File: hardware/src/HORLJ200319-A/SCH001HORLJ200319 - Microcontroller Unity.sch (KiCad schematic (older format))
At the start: 14 parts, among them U1 ATmega328P-MMH, Y1 32.768kHz

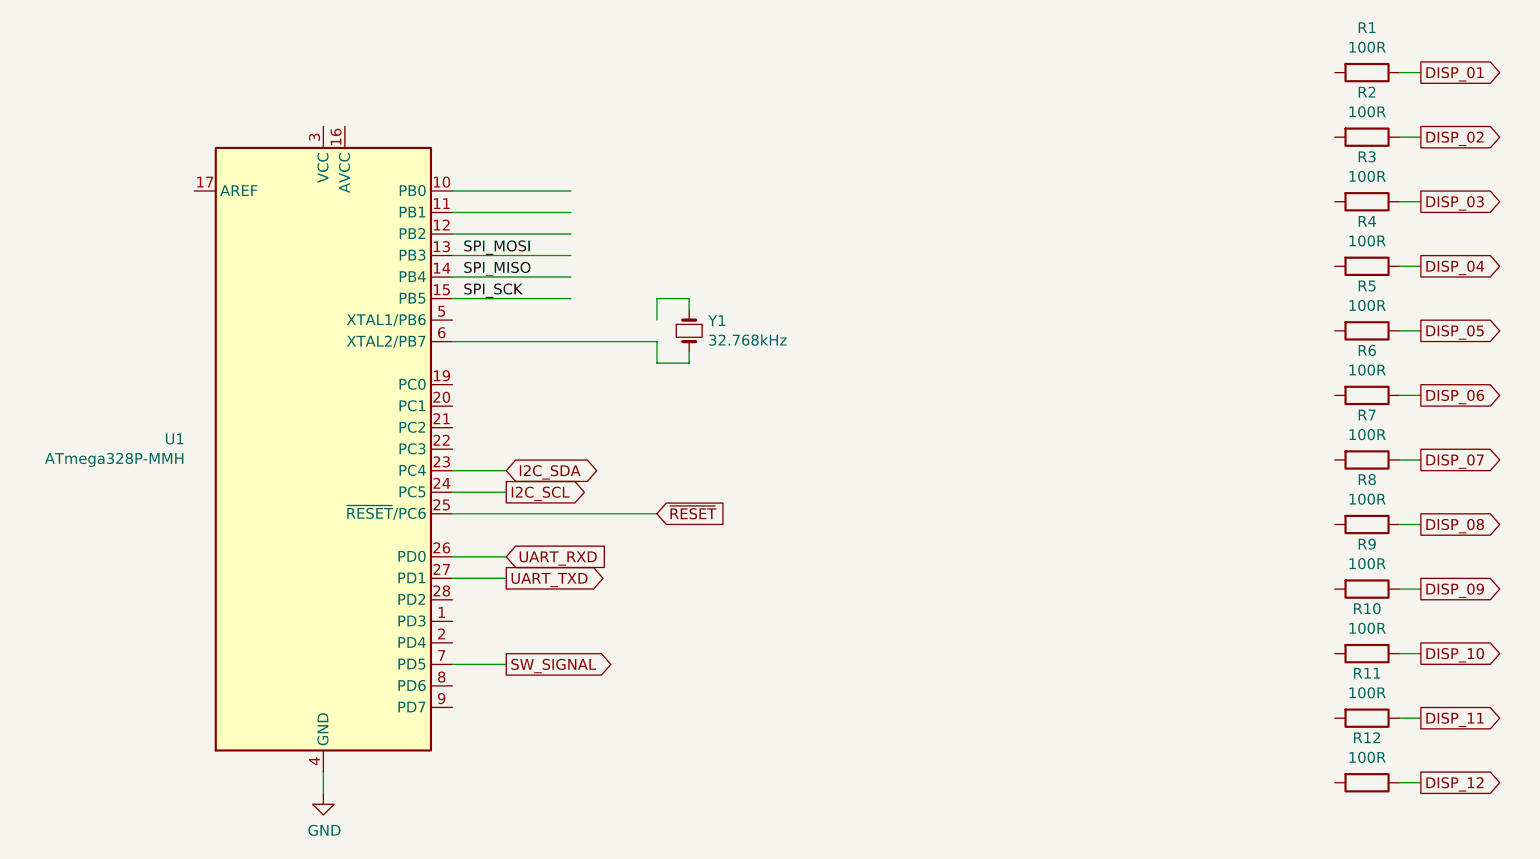
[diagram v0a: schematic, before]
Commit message: Insere MockUps digitais e inicia o projeto da PCB.
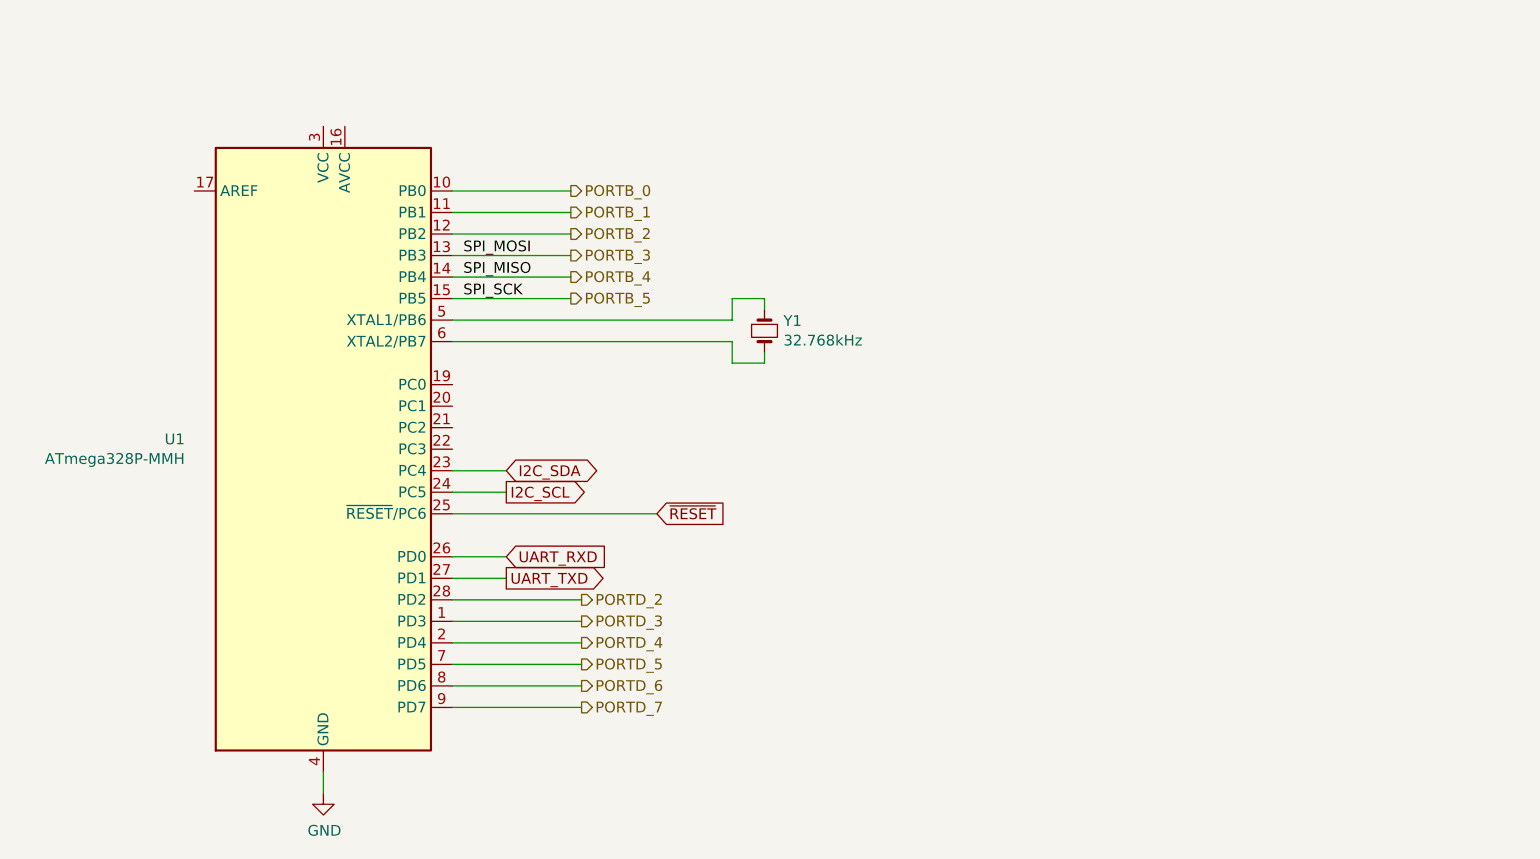
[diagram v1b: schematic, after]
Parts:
- removed R1, R10, R11, R12, R2, R3, R4, R5, R6, R7, R8, R9: 100R, symbol Device:R
- Y1: footprint (none) -> Crystal:Crystal_C26-LF_D2.1mm_L6.5mm_Horizontal
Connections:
- net labels added: PORTB_0, PORTB_1, PORTB_2, PORTB_3, PORTB_4, PORTB_5, PORTD_2, PORTD_3, PORTD_4, PORTD_5, PORTD_6, PORTD_7
- net labels removed: DISP_01, DISP_02, DISP_03, DISP_04, DISP_05, DISP_06, DISP_07, DISP_08, DISP_09, DISP_10, DISP_11, DISP_12, SW_SIGNAL
- wire segments 32 -> 26
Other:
- moved on the sheet: Y1
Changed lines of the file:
@@
 $Descr A4 11693 8268
 encoding utf-8
-Sheet 3 10
+Sheet 2 10
 Title ""
 Date ""
@@
 	1    0    0    -1
 $EndComp
-$Comp
-L Device:Crystal_Small Y1
-U 1 1 5E76C625
-P 5200 3350
-F 0 "Y1" V 5154 3438 50  0000 L CNN
-F 1 "32.768kHz" V 5245 3438 50  0000 L CNN
-F 2 "" H 5200 3350 50  0001 C CNN
-F 3 "~" H 5200 3350 50  0001 C CNN
-	1    5200 3350
-	0    1    1    0
-$EndComp
 Wire Wire Line
-	5050 3300 5050 3200
+	5400 3300 5400 3200
 Wire Wire Line
-	4100 3400 5050 3400
+	4100 3400 5400 3400
 Wire Wire Line
-	5200 3250 5200 3200
+	5550 3200 5400 3200
 Wire Wire Line
-	5200 3200 5050 3200
+	5400 3500 5550 3500
 Wire Wire Line
-	5050 3500 5200 3500
-Wire Wire Line
-	5200 3500 5200 3450
-Wire Wire Line
-	5050 3400 5050 3500
+	5400 3400 5400 3500
 Wire Wire Line
 	4100 4200 5050 4200
@@
 Text GLabel 5050 4200 2    50   Input ~ 0
 ~RESET
-Text GLabel 8600 3050 2    50   Output ~ 0
-DISP_04
-Text GLabel 8600 3350 2    50   Output ~ 0
-DISP_05
-Text GLabel 8600 3650 2    50   Output ~ 0
-DISP_06
 Wire Wire Line
 	4650 3200 4100 3200
@@
 Wire Wire Line
 	4650 3000 4100 3000
-Text GLabel 8600 2150 2    50   Output ~ 0
-DISP_01
 Wire Wire Line
 	4650 2700 4100 2700
-Text GLabel 8600 2450 2    50   Output ~ 0
-DISP_02
 Wire Wire Line
 	4100 2800 4650 2800
-Text GLabel 8600 2750 2    50   Output ~ 0
-DISP_03
 Wire Wire Line
 	4650 2900 4100 2900
@@
 Text Label 4150 3200 0    50   ~ 0
 SPI_SCK
+Text HLabel 4650 2700 2    50   Output ~ 0
+PORTB_0
+Text HLabel 4650 2800 2    50   Output ~ 0
+PORTB_1
+Text HLabel 4650 2900 2    50   Output ~ 0
+PORTB_2
+Text HLabel 4650 3000 2    50   Output ~ 0
+PORTB_3
+Text HLabel 4650 3100 2    50   Output ~ 0
+PORTB_4
+Text HLabel 4650 3200 2    50   Output ~ 0
+PORTB_5
 Wire Wire Line
-	4350 4900 4100 4900
-Text GLabel 4350 4900 2    50   Output ~ 0
-SW_SIGNAL
+	4100 3300 5400 3300
+Wire Wire Line
+	5550 3500 5550 3450
+Wire Wire Line
+	5550 3250 5550 3200
 $Comp
-L Device:R R1
-U 1 1 5E77952B
-P 8350 2150
-F 0 "R1" V 8143 2150 50  0000 C CNN
-F 1 "100R" V 8234 2150 50  0000 C CNN
-F 2 "" V 8280 2150 50  0001 C CNN
-F 3 "~" H 8350 2150 50  0001 C CNN
-	1    8350 2150
+L Device:Crystal_Small Y1
+U 1 1 5E76C625
+P 5550 3350
+F 0 "Y1" V 5504 3438 50  0000 L CNN
+F 1 "32.768kHz" V 5595 3438 50  0000 L CNN
+F 2 "Crystal:Crystal_C26-LF_D2.1mm_L6.5mm_Horizontal" H 5550 3350 50  0001 C CNN
+F 3 "~" H 5550 3350 50  0001 C CNN
+	1    5550 3350
 	0    1    1    0
 $EndComp
+Text HLabel 4700 4600 2    50   Output ~ 0
+PORTD_2
+Text HLabel 4700 4700 2    50   Output ~ 0
+PORTD_3
+Text HLabel 4700 4800 2    50   Output ~ 0
+PORTD_4
+Text HLabel 4700 4900 2    50   Output ~ 0
+PORTD_5
+Text HLabel 4700 5000 2    50   Output ~ 0
+PORTD_6
+Text HLabel 4700 5100 2    50   Output ~ 0
+PORTD_7
 Wire Wire Line
-	8600 2150 8500 2150
-$Comp
-L Device:R R2
-U 1 1 5E779E23
-P 8350 2450
-F 0 "R2" V 8143 2450 50  0000 C CNN
-F 1 "100R" V 8234 2450 50  0000 C CNN
-F 2 "" V 8280 2450 50  0001 C CNN
-F 3 "~" H 8350 2450 50  0001 C CNN
-	1    8350 2450
-	0    1    1    0
-$EndComp
-$Comp
-L Device:R R3
-U 1 1 5E77A0CA
-P 8350 2750
-F 0 "R3" V 8143 2750 50  0000 C CNN
-F 1 "100R" V 8234 2750 50  0000 C CNN
-F 2 "" V 8280 2750 50  0001 C CNN
-F 3 "~" H 8350 2750 50  0001 C CNN
-	1    8350 2750
-	0    1    1    0
-$EndComp
-$Comp
-L Device:R R4
-U 1 1 5E77A366
-P 8350 3050
-F 0 "R4" V 8143 3050 50  0000 C CNN
-F 1 "100R" V 8234 3050 50  0000 C CNN
-F 2 "" V 8280 3050 50  0001 C CNN
-F 3 "~" H 8350 3050 50  0001 C CNN
-	1    8350 3050
-	0    1    1    0
-$EndComp
-$Comp
-L Device:R R5
-U 1 1 5E77A54B
-P 8350 3350
-F 0 "R5" V 8143 3350 50  0000 C CNN
-F 1 "100R" V 8234 3350 50  0000 C CNN
-F 2 "" V 8280 3350 50  0001 C CNN
-F 3 "~" H 8350 3350 50  0001 C CNN
-	1    8350 3350
-	0    1    1    0
-$EndComp
-$Comp
-L Device:R R6
-U 1 1 5E77A820
-P 8350 3650
-F 0 "R6" V 8143 3650 50  0000 C CNN
-F 1 "100R" V 8234 3650 50  0000 C CNN
-F 2 "" V 8280 3650 50  0001 C CNN
-F 3 "~" H 8350 3650 50  0001 C CNN
-	1    8350 3650
-	0    1    1    0
-$EndComp
+	4700 5100 4100 5100
 Wire Wire Line
-	8600 2450 8500 2450
+	4100 5000 4700 5000
 Wire Wire Line
-	8500 2750 8600 2750
+	4700 4900 4100 4900
 Wire Wire Line
-	8600 3050 8500 3050
+	4100 4800 4700 4800
 Wire Wire Line
-	8500 3350 8600 3350
+	4700 4700 4100 4700
 Wire Wire Line
-	8600 3650 8500 3650
-Text GLabel 8600 4850 2    50   Output ~ 0
-DISP_10
-Text GLabel 8600 5150 2    50   Output ~ 0
-DISP_11
-Text GLabel 8600 5450 2    50   Output ~ 0
-DISP_12
-Text GLabel 8600 3950 2    50   Output ~ 0
-DISP_07
-Text GLabel 8600 4250 2    50   Output ~ 0
-DISP_08
-Text GLabel 8600 4550 2    50   Output ~ 0
-DISP_09
-$Comp
-L Device:R R7
-U 1 1 5E78A29C
-P 8350 3950
-F 0 "R7" V 8143 3950 50  0000 C CNN
-F 1 "100R" V 8234 3950 50  0000 C CNN
-F 2 "" V 8280 3950 50  0001 C CNN
-F 3 "~" H 8350 3950 50  0001 C CNN
-	1    8350 3950
-	0    1    1    0
-$EndComp
-Wire Wire Line
-	8600 3950 8500 3950
-$Comp
-L Device:R R8
-U 1 1 5E78A2A3
-P 8350 4250
-F 0 "R8" V 8143 4250 50  0000 C CNN
-F 1 "100R" V 8234 4250 50  0000 C CNN
-F 2 "" V 8280 4250 50  0001 C CNN
-F 3 "~" H 8350 4250 50  0001 C CNN
-	1    8350 4250
-	0    1    1    0
-$EndComp
-$Comp
-L Device:R R9
-U 1 1 5E78A2A9
-P 8350 4550
-F 0 "R9" V 8143 4550 50  0000 C CNN
-F 1 "100R" V 8234 4550 50  0000 C CNN
-F 2 "" V 8280 4550 50  0001 C CNN
-F 3 "~" H 8350 4550 50  0001 C CNN
-	1    8350 4550
-	0    1    1    0
-$EndComp
-$Comp
-L Device:R R10
-U 1 1 5E78A2AF
-P 8350 4850
-F 0 "R10" V 8143 4850 50  0000 C CNN
-F 1 "100R" V 8234 4850 50  0000 C CNN
-F 2 "" V 8280 4850 50  0001 C CNN
-F 3 "~" H 8350 4850 50  0001 C CNN
-	1    8350 4850
-	0    1    1    0
-$EndComp
-$Comp
-L Device:R R11
-U 1 1 5E78A2B5
-P 8350 5150
-F 0 "R11" V 8143 5150 50  0000 C CNN
-F 1 "100R" V 8234 5150 50  0000 C CNN
-F 2 "" V 8280 5150 50  0001 C CNN
-F 3 "~" H 8350 5150 50  0001 C CNN
-	1    8350 5150
-	0    1    1    0
-$EndComp
-$Comp
-L Device:R R12
-U 1 1 5E78A2BB
-P 8350 5450
-F 0 "R12" V 8143 5450 50  0000 C CNN
-F 1 "100R" V 8234 5450 50  0000 C CNN
-F 2 "" V 8280 5450 50  0001 C CNN
-F 3 "~" H 8350 5450 50  0001 C CNN
-	1    8350 5450
-	0    1    1    0
-$EndComp
-Wire Wire Line
-	8600 4250 8500 4250
-Wire Wire Line
-	8500 4550 8600 4550
-Wire Wire Line
-	8600 4850 8500 4850
-Wire Wire Line
-	8500 5150 8600 5150
-Wire Wire Line
-	8600 5450 8500 5450
+	4100 4600 4700 4600
 $EndSCHEMATC

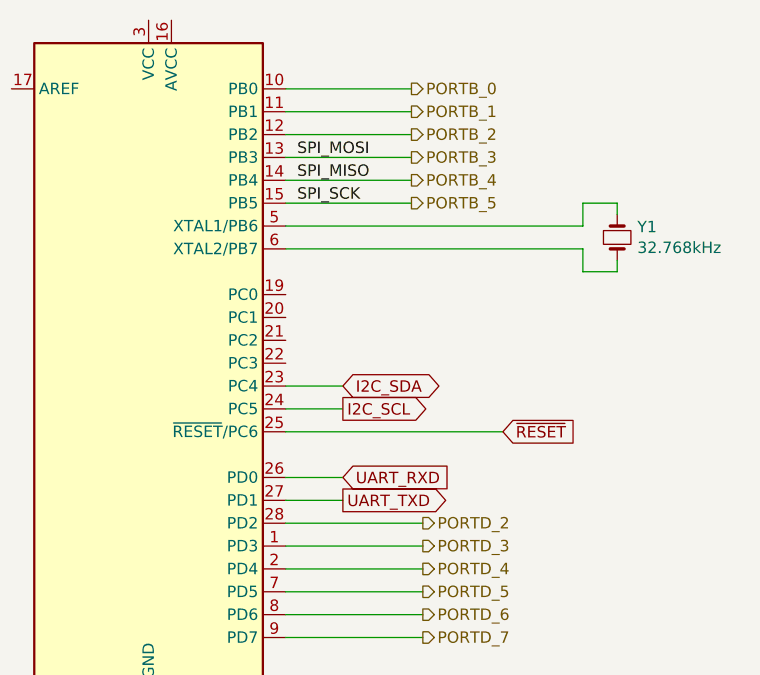
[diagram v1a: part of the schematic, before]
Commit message: Modifica o pinout do MCU.
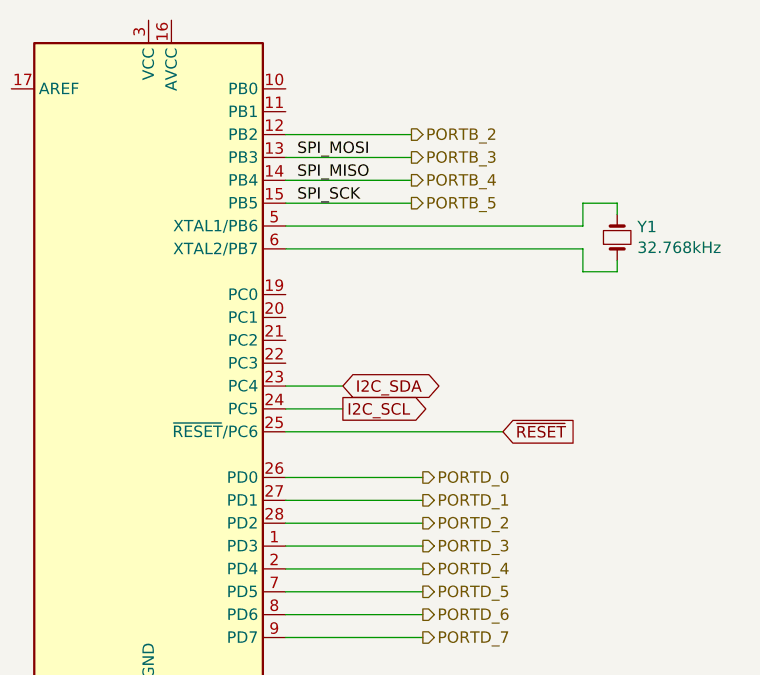
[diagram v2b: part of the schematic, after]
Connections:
- net PORTB_0: no longer names the net of U1.10 (PB0)
- net PORTB_1: no longer names the net of U1.11 (PB1)
- net UART_RXD renamed PORTD_0
- net UART_TXD renamed PORTD_1
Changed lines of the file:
@@
 Wire Wire Line
 	4100 4200 5050 4200
-Text GLabel 4350 4500 2    50   Output ~ 0
-UART_TXD
-Text GLabel 4350 4400 2    50   Input ~ 0
-UART_RXD
 Wire Wire Line
-	4350 4500 4100 4500
+	4700 4500 4100 4500
 Wire Wire Line
-	4100 4400 4350 4400
+	4100 4400 4700 4400
 Text GLabel 4350 4100 2    50   Output ~ 0
 I2C_SCL
@@
 	4650 3000 4100 3000
 Wire Wire Line
-	4650 2700 4100 2700
-Wire Wire Line
-	4100 2800 4650 2800
-Wire Wire Line
 	4650 2900 4100 2900
 Text Label 4150 3000 0    50   ~ 0
@@
 Text Label 4150 3200 0    50   ~ 0
 SPI_SCK
-Text HLabel 4650 2700 2    50   Output ~ 0
-PORTB_0
-Text HLabel 4650 2800 2    50   Output ~ 0
-PORTB_1
+Text HLabel 4700 4400 2    50   Output ~ 0
+PORTD_0
+Text HLabel 4700 4500 2    50   Output ~ 0
+PORTD_1
 Text HLabel 4650 2900 2    50   Output ~ 0
 PORTB_2

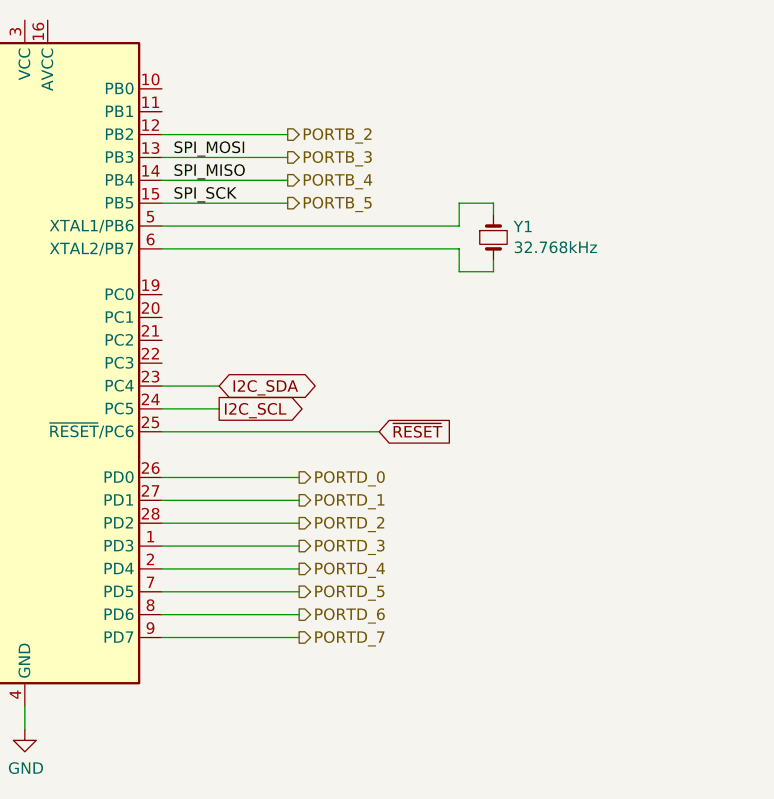
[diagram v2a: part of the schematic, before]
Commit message: Atualiza o pinout do microcontrolador. Implementa arquivo de simulação do hardware.
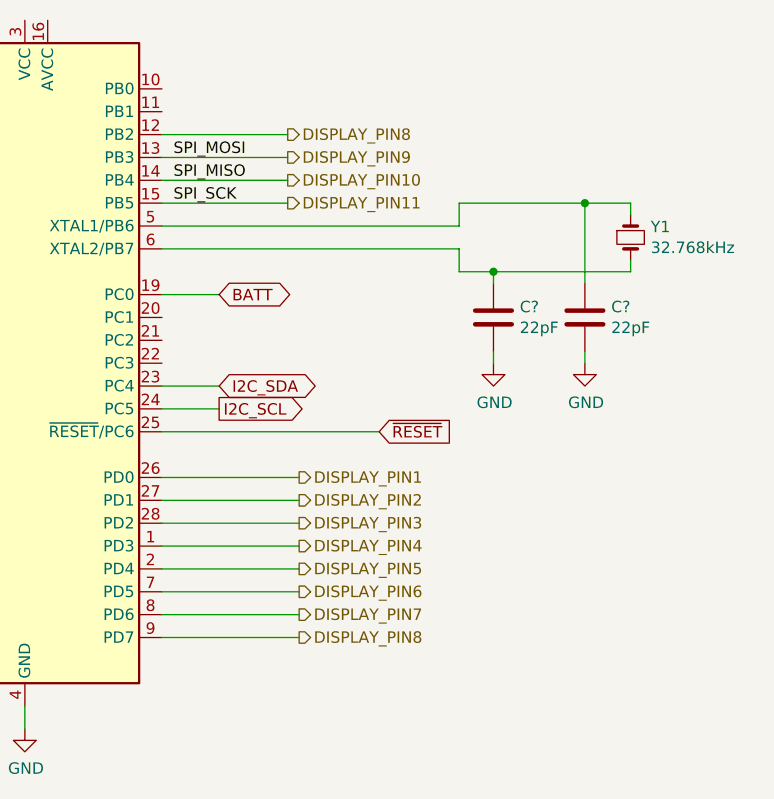
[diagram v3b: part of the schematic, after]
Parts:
- added C? (x2): 22pF, symbol Device:C
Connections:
- net PORTD_7 is gone; now on net DISPLAY_PIN8: U1.9 (PD7)
- net GND: now also C?.2, C?.2
- net BATT: now reaches U1.19 (PC0)
- net at U1.5 (XTAL1/PB6), Y1.1: now also C?.1
- net at U1.6 (XTAL2/PB7), Y1.2: now also C?.1
- net PORTB_2 renamed DISPLAY_PIN8
- net PORTB_3 renamed DISPLAY_PIN9
- net PORTB_4 renamed DISPLAY_PIN10
- net PORTB_5 renamed DISPLAY_PIN11
- net PORTD_0 renamed DISPLAY_PIN1
- net PORTD_1 renamed DISPLAY_PIN2
- net PORTD_2 renamed DISPLAY_PIN3
- net PORTD_3 renamed DISPLAY_PIN4
- net PORTD_4 renamed DISPLAY_PIN5
- net PORTD_5 renamed DISPLAY_PIN6
- net PORTD_6 renamed DISPLAY_PIN7
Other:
- moved on the sheet: Y1
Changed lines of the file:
@@
 $Descr A4 11693 8268
 encoding utf-8
-Sheet 2 10
+Sheet 4 4
 Title ""
 Date ""
@@
 	4100 3400 5400 3400
 Wire Wire Line
-	5550 3200 5400 3200
-Wire Wire Line
-	5400 3500 5550 3500
+	6150 3200 5950 3200
 Wire Wire Line
 	5400 3400 5400 3500
@@
 Wire Wire Line
 	4650 3000 4100 3000
-Wire Wire Line
-	4650 2900 4100 2900
 Text Label 4150 3000 0    50   ~ 0
 SPI_MOSI
@@
 SPI_SCK
 Text HLabel 4700 4400 2    50   Output ~ 0
-PORTD_0
+DISPLAY_PIN1
 Text HLabel 4700 4500 2    50   Output ~ 0
-PORTD_1
+DISPLAY_PIN2
 Text HLabel 4650 2900 2    50   Output ~ 0
-PORTB_2
+DISPLAY_PIN8
 Text HLabel 4650 3000 2    50   Output ~ 0
-PORTB_3
+DISPLAY_PIN9
 Text HLabel 4650 3100 2    50   Output ~ 0
-PORTB_4
+DISPLAY_PIN10
 Text HLabel 4650 3200 2    50   Output ~ 0
-PORTB_5
+DISPLAY_PIN11
 Wire Wire Line
 	4100 3300 5400 3300
 Wire Wire Line
-	5550 3500 5550 3450
+	6150 3500 6150 3450
 Wire Wire Line
-	5550 3250 5550 3200
+	6150 3250 6150 3200
 $Comp
 L Device:Crystal_Small Y1
 U 1 1 5E76C625
-P 5550 3350
-F 0 "Y1" V 5504 3438 50  0000 L CNN
-F 1 "32.768kHz" V 5595 3438 50  0000 L CNN
-F 2 "Crystal:Crystal_C26-LF_D2.1mm_L6.5mm_Horizontal" H 5550 3350 50  0001 C CNN
-F 3 "~" H 5550 3350 50  0001 C CNN
-	1    5550 3350
+P 6150 3350
+F 0 "Y1" V 6104 3438 50  0000 L CNN
+F 1 "32.768kHz" V 6195 3438 50  0000 L CNN
+F 2 "Crystal:Crystal_C26-LF_D2.1mm_L6.5mm_Horizontal" H 6150 3350 50  0001 C CNN
+F 3 "~" H 6150 3350 50  0001 C CNN
+	1    6150 3350
 	0    1    1    0
 $EndComp
 Text HLabel 4700 4600 2    50   Output ~ 0
-PORTD_2
+DISPLAY_PIN3
 Text HLabel 4700 4700 2    50   Output ~ 0
-PORTD_3
+DISPLAY_PIN4
 Text HLabel 4700 4800 2    50   Output ~ 0
-PORTD_4
+DISPLAY_PIN5
 Text HLabel 4700 4900 2    50   Output ~ 0
-PORTD_5
+DISPLAY_PIN6
 Text HLabel 4700 5000 2    50   Output ~ 0
-PORTD_6
+DISPLAY_PIN7
 Text HLabel 4700 5100 2    50   Output ~ 0
-PORTD_7
+DISPLAY_PIN8
 Wire Wire Line
 	4700 5100 4100 5100
@@
 Wire Wire Line
 	4100 4600 4700 4600
+Wire Wire Line
+	5400 3500 5550 3500
+Wire Wire Line
+	4650 2900 4100 2900
+$Comp
+L Device:C C?
+U 1 1 5E92D3C7
+P 5950 3700
+F 0 "C?" H 6065 3746 50  0000 L CNN
+F 1 "22pF" H 6065 3655 50  0000 L CNN
+F 2 "" H 5988 3550 50  0001 C CNN
+F 3 "~" H 5950 3700 50  0001 C CNN
+	1    5950 3700
+	1    0    0    -1
+$EndComp
+$Comp
+L Device:C C?
+U 1 1 5E92E3B1
+P 5550 3700
+F 0 "C?" H 5665 3746 50  0000 L CNN
+F 1 "22pF" H 5665 3655 50  0000 L CNN
+F 2 "" H 5588 3550 50  0001 C CNN
+F 3 "~" H 5550 3700 50  0001 C CNN
+	1    5550 3700
+	1    0    0    -1
+$EndComp
+$Comp
+L power:GND #PWR?
+U 1 1 5E92FBD2
+P 5550 3900
+F 0 "#PWR?" H 5550 3650 50  0001 C CNN
+F 1 "GND" H 5555 3727 50  0000 C CNN
+F 2 "" H 5550 3900 50  0001 C CNN
+F 3 "" H 5550 3900 50  0001 C CNN
+	1    5550 3900
+	1    0    0    -1
+$EndComp
+$Comp
+L power:GND #PWR?
+U 1 1 5E930071
+P 5950 3900
+F 0 "#PWR?" H 5950 3650 50  0001 C CNN
+F 1 "GND" H 5955 3727 50  0000 C CNN
+F 2 "" H 5950 3900 50  0001 C CNN
+F 3 "" H 5950 3900 50  0001 C CNN
+	1    5950 3900
+	1    0    0    -1
+$EndComp
+Wire Wire Line
+	5950 3900 5950 3850
+Wire Wire Line
+	5550 3900 5550 3850
+Wire Wire Line
+	5550 3550 5550 3500
+Connection ~ 5550 3500
+Wire Wire Line
+	5550 3500 6150 3500
+Wire Wire Line
+	5950 3550 5950 3200
+Connection ~ 5950 3200
+Wire Wire Line
+	5950 3200 5400 3200
+Wire Wire Line
+	4350 3600 4100 3600
+Text GLabel 4350 3600 2    50   BiDi ~ 0
+BATT
 $EndSCHEMATC
